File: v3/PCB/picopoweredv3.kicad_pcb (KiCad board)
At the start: 4 copper layers, 39.7 x 56.8 mm, 54 parts, among them J1 Conn_01x03, J5 Micro_SD_Card, J6 Conn_02x11_Odd_Even, J7 Conn_02x11_Odd_Even, P1 USB_C_Plug_USB2.0, SW2 SW_DIP_x03, U1 RP2040, U2 W25Q128JVS, U4 AP2112K-3.3, Y1 ABM8-272-T3

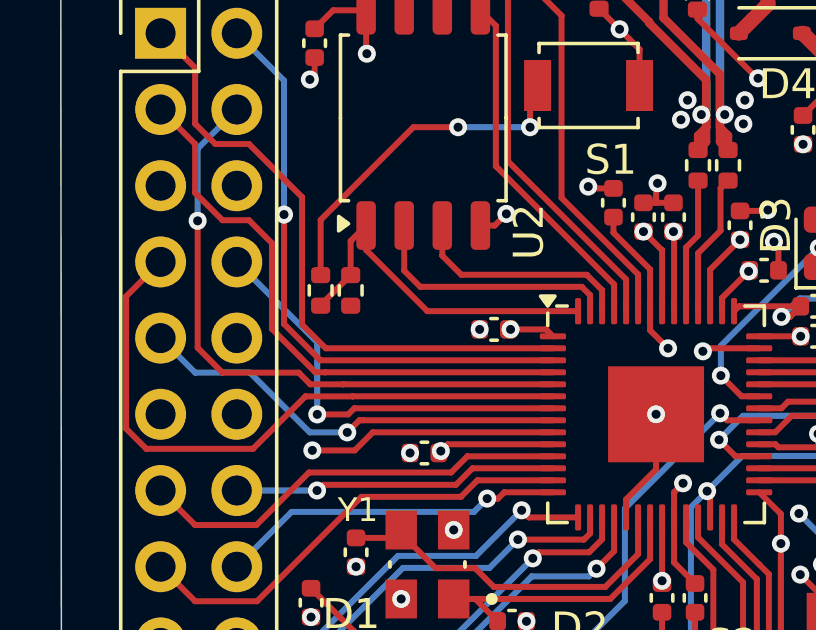
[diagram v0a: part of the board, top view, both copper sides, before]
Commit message: Rename PCB folder and update README
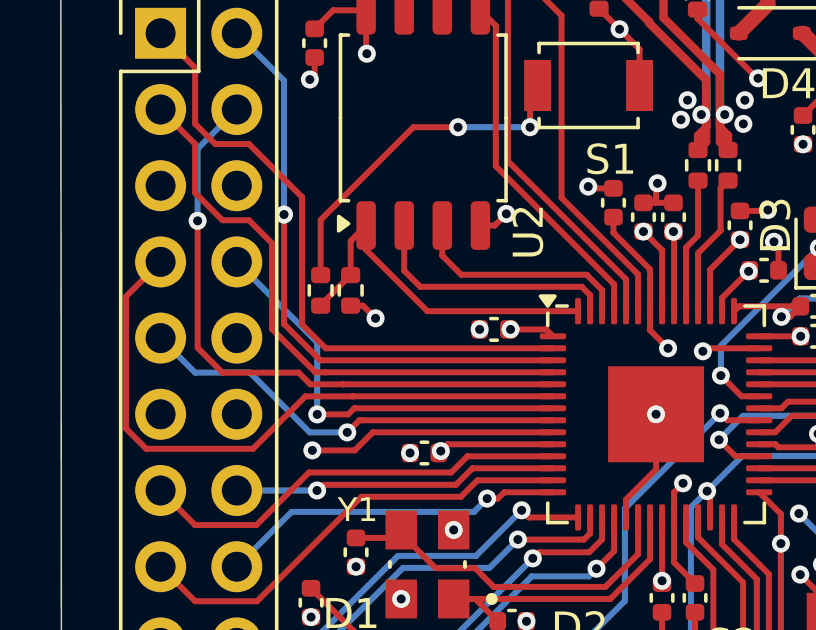
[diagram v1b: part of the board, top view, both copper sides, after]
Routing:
- net +3V3: track 42.5 -> 43.5 mm, vias 18 -> 19
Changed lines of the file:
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@@
 			(outputformat 1)
 			(mirror no)
-			(drillshape 1)
+			(drillshape 0)
 			(scaleselection 1)
-			(outputdirectory "")
+			(outputdirectory "production/")
 		)
 	)
@@
 	)
 	(segment
+		(start 91.83 72.58)
+		(end 92.25 73)
+		(width 0.2)
+		(layer "F.Cu")
+		(net 4)
+	)
+	(segment
 		(start 106.07 72.95)
 		(end 106.42 72.6)
@@
 	)
 	(segment
+		(start 91.42 72.58)
+		(end 91.83 72.58)
+		(width 0.2)
+		(layer "F.Cu")
+		(net 4)
+	)
+	(segment
 		(start 104.66 99.72)
 		(end 104.49 99.89)
@@
 		(size 0.6)
 		(drill 0.3)
+		(layers "F.Cu" "B.Cu")
+		(net 4)
+	)
+	(via
+		(at 92.25 73)
+		(size 0.6)
+		(drill 0.3)
